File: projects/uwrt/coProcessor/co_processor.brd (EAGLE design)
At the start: 101.6 x 101.6 mm, 65 parts

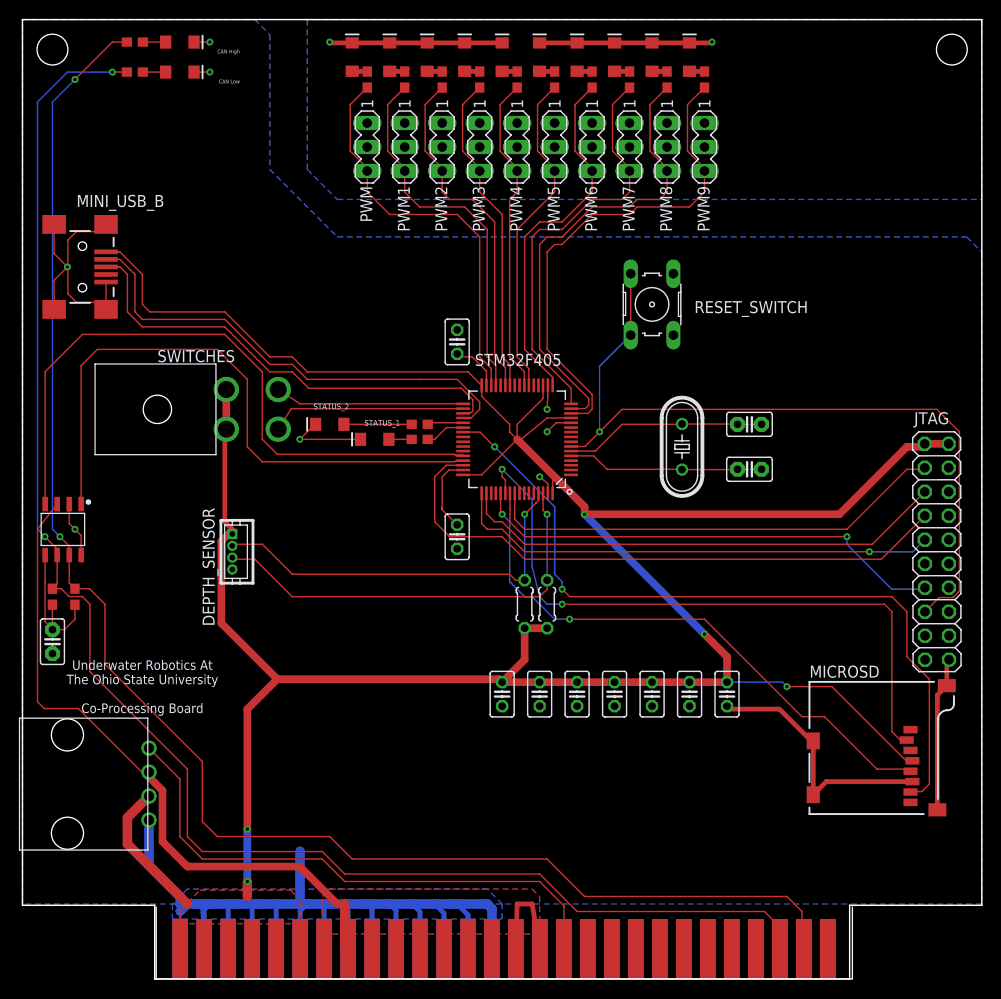
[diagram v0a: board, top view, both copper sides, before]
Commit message: Fixing DRC errors and approving others
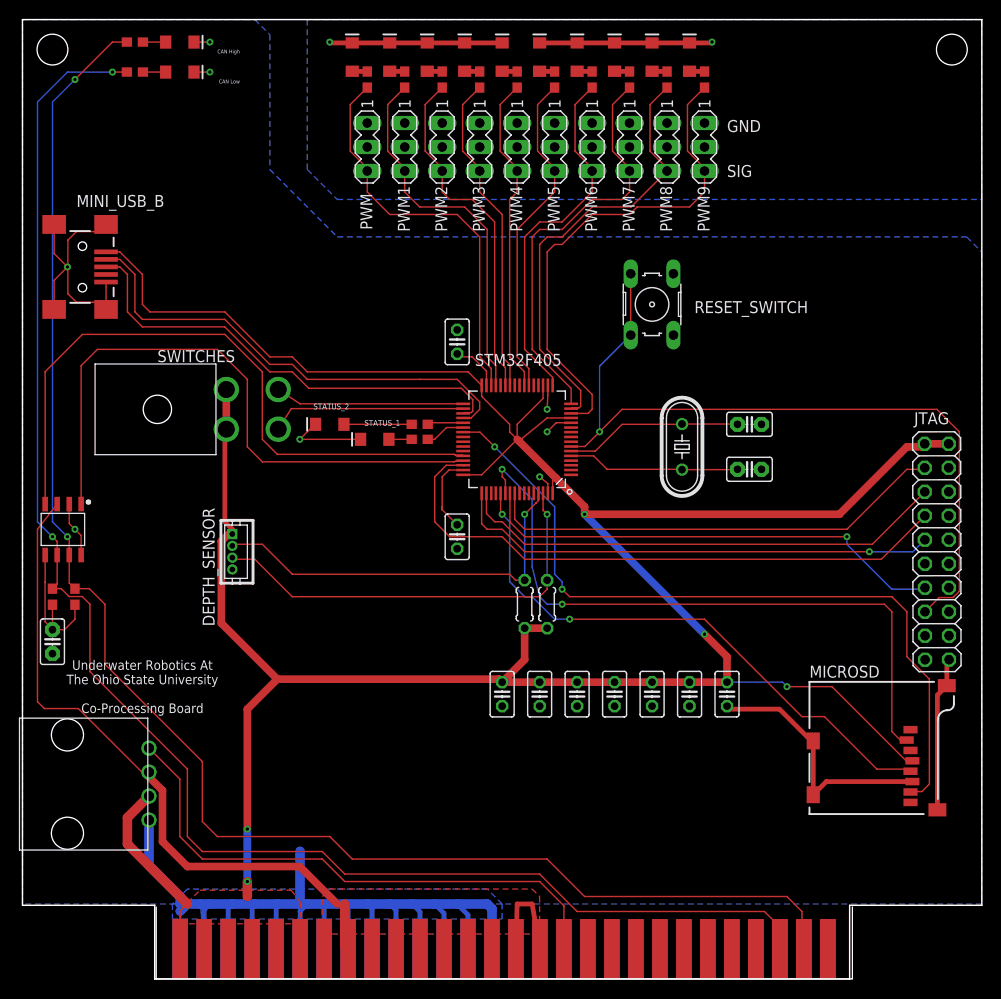
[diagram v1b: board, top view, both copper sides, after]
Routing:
- net PWM8_OUT: track 49.5 -> 47.1 mm
- net CANH_OUT: track 164.8 -> 165.7 mm
- net CANL_OUT: track 166.0 -> 166.6 mm
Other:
- board text added: "GND"
- board text added: "SIG"

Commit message: No frills Co Processing board rev 1.1.0
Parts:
- added BIAS_R, BIAS_R1, BIAS_R2, BIAS_R3, BIAS_R4, BIAS_R5, BIAS_R6, BIAS_R7, BIAS_R8, BIAS_R9: 1K, SparkFun-Resistors:0603
- added OPI_PWM0, OPI_PWM1, OPI_PWM2, OPI_PWM3, OPI_PWM4, OPI_PWM5, OPI_PWM6, OPI_PWM7, OPI_PWM8, OPI_PWM9: SFH610, SFH610:DIL04
- added PWM_IN0, PWM_IN1, PWM_IN2, PWM_IN3, PWM_IN4, PWM_IN5, PWM_IN6, PWM_IN7, PWM_IN8, PWM_IN9: 330, SparkFun-Resistors:0603
- moved C12 42.4 mm to (32.5, 63.5), turned to 90 degrees
- moved C10 36.3 mm to (69.8, 61.1), turned to 90 degrees
- moved C15 31.2 mm to (66.7, 61.1), turned to 90 degrees
- moved C13 31.0 mm to (63.5, 61.1), turned to 90 degrees
- moved RESET_SWITCH 21.8 mm to (84.9, 59.5)
- moved C9 19.2 mm to (65.1, 46.8), turned to 90 degrees
- moved C11 18.0 mm to (42.1, 42.9)
- moved C14 17.3 mm to (61.9, 46.8), turned to 90 degrees
- moved C8 10.3 mm to (36.5, 63.5)
- moved PWM_R9 4.76 mm to (77.0, 95.2)
- moved MICROSD 4.76 mm to (83.3, 12.7)
- moved R2 4.27 mm to (51.6, 35.7)
- moved C7 3.97 mm to (46.0, 42.9)
- moved CANH_OUT_R 3.97 mm to (5.56, 36.5)
- moved CANL_OUT_R 3.97 mm to (3.17, 36.5)
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- renumbered PWM to P0, PWM1 to P1, PWM2 to P2, PWM3 to P3, PWM4 to P4, PWM5 to P5, PWM6 to P6, PWM7 to P7, PWM8 to P8, PWM9 to P9
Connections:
- new net N$10: OPI_PWM4.1, PWM_IN4.2
- new net N$11: OPI_PWM5.1, PWM_IN5.2
- new net N$17: OPI_PWM9.1, PWM_IN9.2
- new net N$23: OPI_PWM6.1, PWM_IN6.2
- new net N$24: OPI_PWM7.1, PWM_IN7.2
- new net N$25: OPI_PWM8.1, PWM_IN8.2
- new net N$29: OPI_PWM0.1, PWM_IN0.2
- new net N$47: OPI_PWM2.1, PWM_IN2.2
- new net N$6: OPI_PWM1.1, PWM_IN1.2
- new net N$9: OPI_PWM3.1, PWM_IN3.2
- new net PWM0_BO: BIAS_R.1, OPI_PWM0.3, P0.3, PWM_R.1
- new net PWM1_BO: BIAS_R1.1, OPI_PWM1.3, P1.3, PWM_R1.1
- new net PWM2_BO: BIAS_R2.1, OPI_PWM2.3, P2.3, PWM_R2.1
- new net PWM3_BO: BIAS_R3.1, OPI_PWM3.3, P3.3, PWM_R3.1
- new net PWM4_BO: BIAS_R4.1, OPI_PWM4.3, P4.3, PWM_R4.1
- new net PWM5_BO: BIAS_R5.1, OPI_PWM5.3, P5.3, PWM_R5.1
- new net PWM6_BO: BIAS_R6.1, OPI_PWM6.3, P6.3, PWM_R6.1
- new net PWM7_BO: BIAS_R7.1, OPI_PWM7.3, P7.3, PWM_R7.1
- new net PWM8_BO: BIAS_R8.1, OPI_PWM8.3, P8.3, PWM_R8.1
- new net PWM9_BO: BIAS_R9.1, OPI_PWM9.3, P9.3, PWM_R9.1
- net 12V_OUT: now also BIAS_R.2, BIAS_R1.2, BIAS_R2.2, BIAS_R3.2, BIAS_R4.2, BIAS_R5.2, BIAS_R6.2, BIAS_R7.2, BIAS_R8.2, BIAS_R9.2
- net GND: now also OPI_PWM0.2, OPI_PWM1.2, OPI_PWM2.2, OPI_PWM3.2, OPI_PWM4.2, OPI_PWM5.2, OPI_PWM6.2, OPI_PWM7.2, OPI_PWM8.2, OPI_PWM9.2; no longer MICROSD.CD1, MICROSD.CD2
- net GND_ESC: now also OPI_PWM0.4, OPI_PWM1.4, OPI_PWM2.4, OPI_PWM3.4, OPI_PWM4.4, OPI_PWM5.4, OPI_PWM6.4, OPI_PWM7.4, OPI_PWM8.4, OPI_PWM9.4
- net PWM0_OUT: now also PWM_IN0.1; no longer P0.3, PWM_R.1
- net PWM1_OUT: now also PWM_IN1.1; no longer P1.3, PWM_R1.1
- net PWM2_OUT: now also PWM_IN2.1; no longer P2.3, PWM_R2.1
- net PWM3_OUT: now also PWM_IN3.1; no longer P3.3, PWM_R3.1
- net PWM4_OUT: now also PWM_IN4.1; no longer P4.3, PWM_R4.1
- net PWM5_OUT: now also PWM_IN5.1; no longer P5.3, PWM_R5.1
- net PWM6_OUT: now also PWM_IN6.1; no longer P6.3, PWM_R6.1
- net PWM7_OUT: now also PWM_IN7.1; no longer P7.3, PWM_R7.1
- net PWM8_OUT: now also PWM_IN8.1; no longer P8.3, PWM_R8.1
- net PWM9_OUT: now also PWM_IN9.1; no longer P9.3, PWM_R9.1
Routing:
- net 12V_OUT: track 59.0 -> 207.1 mm, vias 0 -> 13
- net +3V3: track 312.3 -> 424.9 mm, vias 5 -> 6
- net PWM7_OUT: track 44.2 -> 6.30 mm
- net PWM6_OUT: track 38.6 -> 4.17 mm
- net PWM9_BO: track 0.00 -> 32.2 mm
- net PWM5_OUT: track 35.2 -> 4.22 mm
- net PWM4_OUT: track 34.0 -> 4.07 mm
- net PWM8_BO: track 0.00 -> 28.8 mm
- net PWM0_OUT: track 42.7 -> 14.1 mm
- net PWM1_OUT: track 39.8 -> 11.9 mm
- net GND: track 221.2 -> 193.3 mm, vias 8 -> 9
- net PWM2_OUT: track 37.2 -> 10.0 mm
- net PWM7_BO: track 0.00 -> 26.8 mm
- net PWM3_OUT: track 34.4 -> 8.91 mm
- net PWM9_OUT: track 52.9 -> 27.7 mm
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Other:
- board text added: "Kill"
- board text added: "Start"

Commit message: Small updates before transfer of ownership
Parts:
- removed BIAS_R: 1K, SparkFun-Resistors:0603
- removed PWM_LED, PWM_LED1, PWM_LED2, PWM_LED3, PWM_LED4, PWM_LED5, PWM_LED6, PWM_LED7, PWM_LED8, PWM_LED9: (no value), SparkFun-LED:LED-1206
- removed PWM_R, PWM_R1, PWM_R2, PWM_R3, PWM_R4, PWM_R5, PWM_R6, PWM_R7, PWM_R8, PWM_R9: 330, SparkFun-Resistors:0603
- added BIAS_R0: 1K, SparkFun-Resistors:0603
- moved BIAS_R9 24.0 mm to (72.2, 95.2), flipped to the top, turned to 90 degrees
- moved BIAS_R8 22.7 mm to (68.3, 95.2), flipped to the top, turned to 90 degrees
- moved BIAS_R7 21.7 mm to (64.3, 95.2), flipped to the top, turned to 90 degrees
- moved BIAS_R6 20.8 mm to (60.3, 95.2), flipped to the top, turned to 90 degrees
- moved BIAS_R1 20.6 mm to (40.5, 95.2), flipped to the top, turned to 90 degrees
- moved BIAS_R5 20.2 mm to (56.4, 95.2), flipped to the top, turned to 90 degrees
- moved BIAS_R2 20.1 mm to (44.5, 95.2), flipped to the top
- moved BIAS_R4 19.9 mm to (52.4, 95.2), flipped to the top, turned to 90 degrees
- moved BIAS_R3 19.9 mm to (48.4, 95.2), flipped to the top, turned to 90 degrees
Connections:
- removed net N$13: PWM_LED2.A, PWM_R2.2
- removed net N$14: PWM_LED3.A, PWM_R3.2
- removed net N$18: PWM_LED9.A, PWM_R9.2
- removed net N$19: PWM_LED8.A, PWM_R8.2
- removed net N$20: PWM_LED7.A, PWM_R7.2
- removed net N$21: PWM_LED6.A, PWM_R6.2
- removed net N$22: PWM_LED5.A, PWM_R5.2
- removed net N$26: PWM_LED4.A, PWM_R4.2
- removed net N$7: PWM_LED.A, PWM_R.2
- removed net N$8: PWM_LED1.A, PWM_R1.2
- removed net PWM0_BO: BIAS_R.1, OPI_PWM0.3, P0.3, PWM_R.1
- removed net PWM1_BO: BIAS_R1.1, OPI_PWM1.3, P1.3, PWM_R1.1
- removed net PWM2_BO: BIAS_R2.1, OPI_PWM2.3, P2.3, PWM_R2.1
- removed net PWM3_BO: BIAS_R3.1, OPI_PWM3.3, P3.3, PWM_R3.1
- removed net PWM4_BO: BIAS_R4.1, OPI_PWM4.3, P4.3, PWM_R4.1
- removed net PWM5_BO: BIAS_R5.1, OPI_PWM5.3, P5.3, PWM_R5.1
- removed net PWM6_BO: BIAS_R6.1, OPI_PWM6.3, P6.3, PWM_R6.1
- removed net PWM7_BO: BIAS_R7.1, OPI_PWM7.3, P7.3, PWM_R7.1
- removed net PWM8_BO: BIAS_R8.1, OPI_PWM8.3, P8.3, PWM_R8.1
- removed net PWM9_BO: BIAS_R9.1, OPI_PWM9.3, P9.3, PWM_R9.1
- new net EMIT0: BIAS_R0.1, OPI_PWM0.4, P0.1
- new net EMIT1: BIAS_R1.1, OPI_PWM1.4, P1.1
- new net EMIT2: BIAS_R2.2, OPI_PWM2.4, P2.1
- new net EMIT3: BIAS_R3.1, OPI_PWM3.4, P3.1
- new net EMIT4: BIAS_R4.1, OPI_PWM4.4, P4.1
- new net EMIT5: BIAS_R5.1, OPI_PWM5.4, P5.1
- new net EMIT6: BIAS_R6.1, OPI_PWM6.4, P6.1
- new net EMIT7: BIAS_R7.1, OPI_PWM7.4, P7.1
- new net EMIT8: BIAS_R8.1, OPI_PWM8.4, P8.1
- new net EMIT9: BIAS_R9.1, OPI_PWM9.4, P9.1
- net 12V_OUT: now also OPI_PWM0.3, OPI_PWM1.3, OPI_PWM2.3, OPI_PWM3.3, OPI_PWM4.3, OPI_PWM5.3, OPI_PWM6.3, OPI_PWM7.3, OPI_PWM8.3, OPI_PWM9.3, P0.3, P1.3, P2.3, P3.3, P4.3, P5.3, P6.3, P7.3, P8.3, P9.3; no longer BIAS_R.2, BIAS_R1.2, BIAS_R2.2, BIAS_R3.2, BIAS_R4.2, BIAS_R5.2, BIAS_R6.2, BIAS_R7.2, BIAS_R8.2, BIAS_R9.2
- net GND_ESC: now also BIAS_R0.2, BIAS_R1.2, BIAS_R2.1, BIAS_R3.2, BIAS_R4.2, BIAS_R5.2, BIAS_R6.2, BIAS_R7.2, BIAS_R8.2, BIAS_R9.2; no longer OPI_PWM0.4, OPI_PWM1.4, OPI_PWM2.4, OPI_PWM3.4, OPI_PWM4.4, OPI_PWM5.4, OPI_PWM6.4, OPI_PWM7.4, OPI_PWM8.4, OPI_PWM9.4, P0.1, P1.1, P2.1, P3.1, P4.1, P5.1, P6.1, P7.1, P8.1, P9.1, PWM_LED.C, PWM_LED1.C, PWM_LED2.C, PWM_LED3.C, PWM_LED4.C, PWM_LED5.C, PWM_LED6.C, PWM_LED7.C, PWM_LED8.C, PWM_LED9.C
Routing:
- net 12V_OUT: track 207.1 -> 325.7 mm, vias 13 -> 12
- net PWM9_BO: track 32.2 -> 0.00 mm
- net PWM8_BO: track 28.8 -> 0.00 mm
- net EMIT9: track 0.00 -> 28.8 mm
- net PWM7_BO: track 26.8 -> 0.00 mm
- net EMIT8: track 0.00 -> 24.8 mm
- net PWM6_BO: track 23.8 -> 0.00 mm
- net EMIT7: track 0.00 -> 23.4 mm
- net PWM0_BO: track 22.4 -> 0.00 mm
- net PWM4_BO: track 21.7 -> 0.00 mm
- net PWM5_BO: track 21.7 -> 0.00 mm
- net PWM1_BO: track 21.3 -> 0.00 mm
- net EMIT6: track 0.00 -> 21.0 mm
- net EMIT0: track 0.00 -> 20.7 mm
- net PWM2_BO: track 20.6 -> 0.00 mm
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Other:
- board text added: "PWM0"
- board text added: "PWM1"
- board text added: "PWM2"
- board text added: "PWM3"
- board text added: "PWM4"
- board text added: "PWM5"
- board text added: "PWM6"
- board text added: "PWM7"
- board text added: "PWM8"
- board text added: "PWM9"
